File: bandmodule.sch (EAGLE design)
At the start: 16 parts

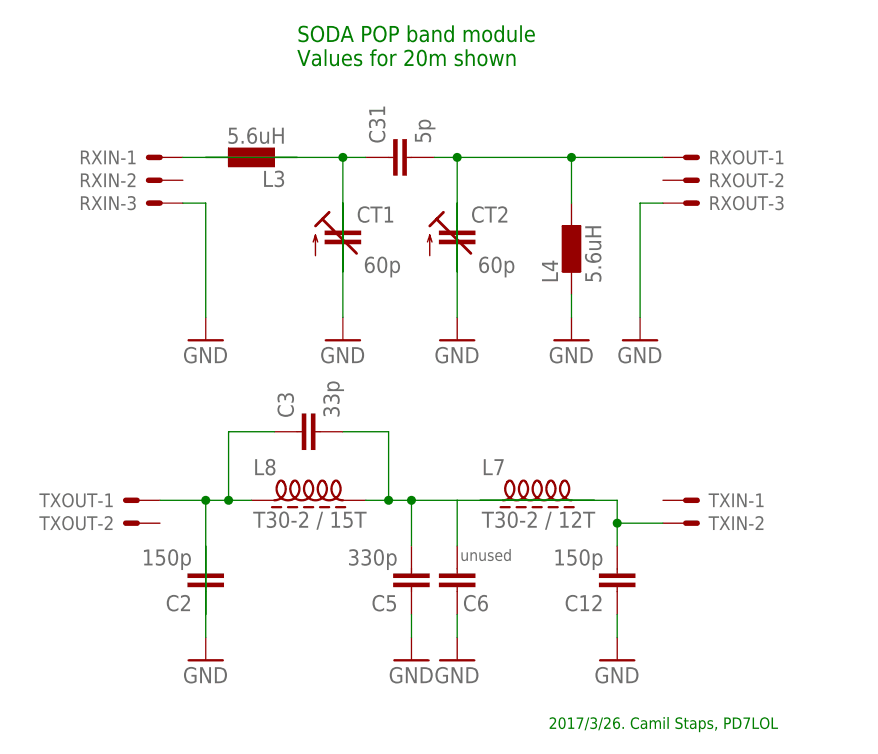
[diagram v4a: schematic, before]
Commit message: Merge C5 and C6 again
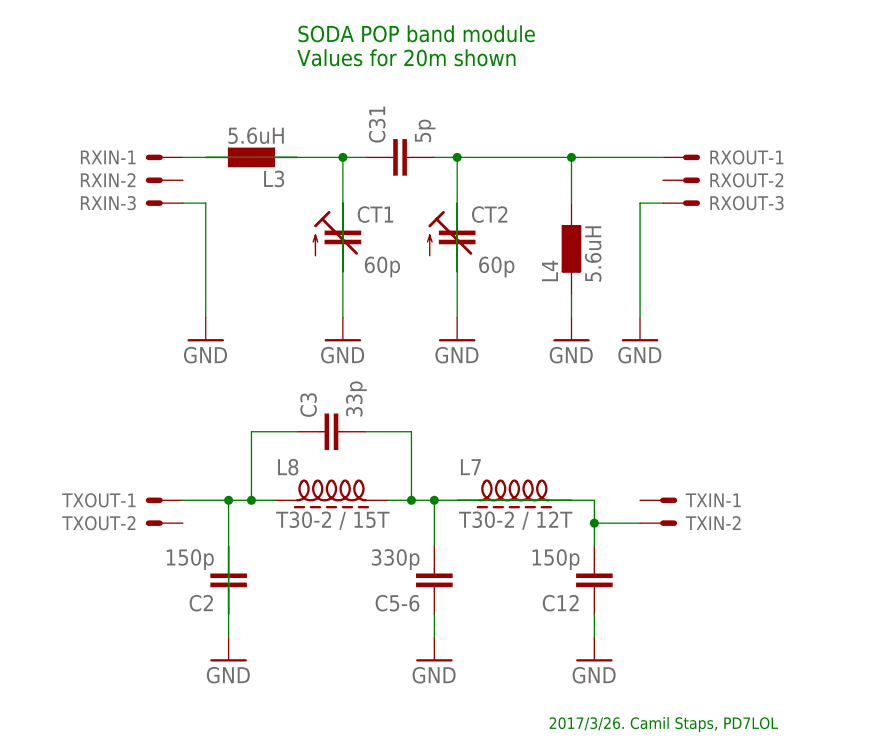
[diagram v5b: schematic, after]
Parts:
- removed C5: 330p, capacitor-wima:C5/2.5
- removed C6: unused, capacitor-wima:C5/2.5
- added C5-6: 330p, capacitor-wima:C5/2.5
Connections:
- net GND: now also C5-6.1; no longer C5.1, C6.1
- net N$5: now also C5-6.2; no longer C5.2, C6.2
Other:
- moved on the sheet: C12, C2, C3, L7, L8, TXIN-1, TXIN-2, TXOUT-1, TXOUT-2
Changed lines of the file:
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@@
 <part name="L8" library="toroids" deviceset="INDUCTOR" device="T30-2-28AWG-12T" value="T30-2 / 15T"/>
 <part name="L7" library="toroids" deviceset="INDUCTOR" device="T30-2-28AWG-12T" value="T30-2 / 12T"/>
-<part name="C5" library="capacitor-wima" deviceset="C" device="5/2.5" value="330p"/>
+<part name="C5-6" library="capacitor-wima" deviceset="C" device="5/2.5" value="330p"/>
 <part name="C12" library="capacitor-wima" deviceset="C" device="5/2.5" value="150p"/>
 <part name="C3" library="capacitor-wima" deviceset="C" device="5/2.5" value="33p"/>
@@
 <part name="L4" library="eagle-ltspice" deviceset="L" device="0207/10" value="5.6uH"/>
 <part name="L3" library="eagle-ltspice" deviceset="L" device="0207/10" value="5.6uH"/>
-<part name="C6" library="capacitor-wima" deviceset="C" device="5/2.5" value="unused"/>
-<part name="GND9" library="supply1" deviceset="GND" device=""/>
 </parts>
 <sheets>
@@
 <instance part="GND4" gate="1" x="48.26" y="45.72"/>
 <instance part="GND5" gate="1" x="60.96" y="45.72"/>
-<instance part="TXIN" gate="-1" x="73.66" y="27.94" smashed="yes">
-<attribute name="NAME" x="76.2" y="27.178" size="1.524" layer="95"/>
+<instance part="TXIN" gate="-1" x="71.12" y="27.94" smashed="yes">
+<attribute name="NAME" x="73.66" y="27.178" size="1.524" layer="95"/>
 </instance>
-<instance part="TXIN" gate="-2" x="73.66" y="25.4"/>
-<instance part="TXOUT" gate="-1" x="12.7" y="27.94" smashed="yes" rot="MR0">
-<attribute name="NAME" x="10.16" y="27.178" size="1.524" layer="95" rot="MR0"/>
+<instance part="TXIN" gate="-2" x="71.12" y="25.4"/>
+<instance part="TXOUT" gate="-1" x="15.24" y="27.94" smashed="yes" rot="MR0">
+<attribute name="NAME" x="12.7" y="27.178" size="1.524" layer="95" rot="MR0"/>
 </instance>
-<instance part="TXOUT" gate="-2" x="12.7" y="25.4" rot="MR0"/>
-<instance part="C2" gate="G$1" x="20.32" y="17.78" rot="R180"/>
-<instance part="L8" gate="G$1" x="30.48" y="27.94"/>
-<instance part="L7" gate="G$1" x="55.88" y="27.94"/>
-<instance part="C5" gate="G$1" x="43.18" y="17.78" smashed="yes" rot="R180">
-<attribute name="NAME" x="41.656" y="17.399" size="1.778" layer="95" rot="R180"/>
-<attribute name="VALUE" x="41.656" y="22.479" size="1.778" layer="96" rot="R180"/>
+<instance part="TXOUT" gate="-2" x="15.24" y="25.4" rot="MR0"/>
+<instance part="C2" gate="G$1" x="22.86" y="17.78" rot="R180"/>
+<instance part="L8" gate="G$1" x="33.02" y="27.94"/>
+<instance part="L7" gate="G$1" x="53.34" y="27.94"/>
+<instance part="C5-6" gate="G$1" x="45.72" y="17.78" smashed="yes" rot="R180">
+<attribute name="NAME" x="44.196" y="17.399" size="1.778" layer="95" rot="R180"/>
+<attribute name="VALUE" x="44.196" y="22.479" size="1.778" layer="96" rot="R180"/>
 </instance>
-<instance part="C12" gate="G$1" x="66.04" y="17.78" rot="R180"/>
-<instance part="C3" gate="G$1" x="30.48" y="35.56" rot="R90"/>
-<instance part="GND6" gate="1" x="20.32" y="10.16"/>
-<instance part="GND7" gate="1" x="43.18" y="10.16"/>
-<instance part="GND8" gate="1" x="66.04" y="10.16"/>
+<instance part="C12" gate="G$1" x="63.5" y="17.78" rot="R180"/>
+<instance part="C3" gate="G$1" x="33.02" y="35.56" rot="R90"/>
+<instance part="GND6" gate="1" x="22.86" y="10.16"/>
+<instance part="GND7" gate="1" x="45.72" y="10.16"/>
+<instance part="GND8" gate="1" x="63.5" y="10.16"/>
 <instance part="L4" gate="G$1" x="60.96" y="55.88"/>
 <instance part="L3" gate="G$1" x="25.4" y="66.04" rot="R90"/>
-<instance part="C6" gate="G$1" x="48.26" y="17.78" smashed="yes" rot="R180">
-<attribute name="NAME" x="51.816" y="17.399" size="1.778" layer="95" rot="R180"/>
-<attribute name="VALUE" x="54.356" y="22.479" size="1.27" layer="96" rot="R180"/>
-</instance>
-<instance part="GND9" gate="1" x="48.26" y="10.16"/>
 </instances>
 <busses>
@@
 <pinref part="C2" gate="G$1" pin="2"/>
 <pinref part="GND6" gate="1" pin="GND"/>
-<wire x1="20.32" y1="22.86" x2="20.32" y2="12.7" width="0.1524" layer="91"/>
+<wire x1="22.86" y1="22.86" x2="22.86" y2="12.7" width="0.1524" layer="91"/>
 </segment>
 <segment>
-<pinref part="C5" gate="G$1" pin="1"/>
+<pinref part="C5-6" gate="G$1" pin="1"/>
 <pinref part="GND7" gate="1" pin="GND"/>
-<wire x1="43.18" y1="15.24" x2="43.18" y2="12.7" width="0.1524" layer="91"/>
+<wire x1="45.72" y1="15.24" x2="45.72" y2="12.7" width="0.1524" layer="91"/>
 </segment>
 <segment>
 <pinref part="C12" gate="G$1" pin="1"/>
 <pinref part="GND8" gate="1" pin="GND"/>
-<wire x1="66.04" y1="15.24" x2="66.04" y2="12.7" width="0.1524" layer="91"/>
-</segment>
-<segment>
-<pinref part="GND9" gate="1" pin="GND"/>
-<pinref part="C6" gate="G$1" pin="1"/>
-<wire x1="48.26" y1="12.7" x2="48.26" y2="15.24" width="0.1524" layer="91"/>
+<wire x1="63.5" y1="15.24" x2="63.5" y2="12.7" width="0.1524" layer="91"/>
 </segment>
 </net>
@@
 <pinref part="L8" gate="G$1" pin="2"/>
 <pinref part="L7" gate="G$1" pin="2"/>
-<wire x1="38.1" y1="27.94" x2="40.64" y2="27.94" width="0.1524" layer="91"/>
-<pinref part="C5" gate="G$1" pin="2"/>
 <wire x1="40.64" y1="27.94" x2="43.18" y2="27.94" width="0.1524" layer="91"/>
-<wire x1="43.18" y1="27.94" x2="48.26" y2="27.94" width="0.1524" layer="91"/>
-<wire x1="48.26" y1="27.94" x2="63.5" y2="27.94" width="0.1524" layer="91"/>
-<wire x1="43.18" y1="27.94" x2="43.18" y2="22.86" width="0.1524" layer="91"/>
+<pinref part="C5-6" gate="G$1" pin="2"/>
+<wire x1="43.18" y1="27.94" x2="45.72" y2="27.94" width="0.1524" layer="91"/>
+<wire x1="45.72" y1="27.94" x2="60.96" y2="27.94" width="0.1524" layer="91"/>
+<wire x1="45.72" y1="27.94" x2="45.72" y2="22.86" width="0.1524" layer="91"/>
 <pinref part="C3" gate="G$1" pin="2"/>
-<wire x1="35.56" y1="35.56" x2="40.64" y2="35.56" width="0.1524" layer="91"/>
-<wire x1="40.64" y1="35.56" x2="40.64" y2="27.94" width="0.1524" layer="91"/>
-<junction x="40.64" y="27.94"/>
+<wire x1="38.1" y1="35.56" x2="43.18" y2="35.56" width="0.1524" layer="91"/>
+<wire x1="43.18" y1="35.56" x2="43.18" y2="27.94" width="0.1524" layer="91"/>
 <junction x="43.18" y="27.94"/>
-<pinref part="C6" gate="G$1" pin="2"/>
-<wire x1="48.26" y1="22.86" x2="48.26" y2="27.94" width="0.1524" layer="91"/>
+<junction x="45.72" y="27.94"/>
 </segment>
 </net>
@@
 <pinref part="L7" gate="G$1" pin="1"/>
 <pinref part="C12" gate="G$1" pin="2"/>
-<wire x1="50.8" y1="27.94" x2="66.04" y2="27.94" width="0.1524" layer="91"/>
-<wire x1="66.04" y1="27.94" x2="66.04" y2="25.4" width="0.1524" layer="91"/>
+<wire x1="48.26" y1="27.94" x2="63.5" y2="27.94" width="0.1524" layer="91"/>
+<wire x1="63.5" y1="27.94" x2="63.5" y2="25.4" width="0.1524" layer="91"/>
 <pinref part="TXIN" gate="-2" pin="S"/>
-<wire x1="66.04" y1="25.4" x2="66.04" y2="22.86" width="0.1524" layer="91"/>
-<wire x1="66.04" y1="25.4" x2="71.12" y2="25.4" width="0.1524" layer="91"/>
-<junction x="66.04" y="25.4"/>
+<wire x1="63.5" y1="25.4" x2="63.5" y2="22.86" width="0.1524" layer="91"/>
+<wire x1="63.5" y1="25.4" x2="68.58" y2="25.4" width="0.1524" layer="91"/>
+<junction x="63.5" y="25.4"/>
 </segment>
 </net>
@@
 <segment>
 <pinref part="C3" gate="G$1" pin="1"/>
-<wire x1="22.86" y1="35.56" x2="27.94" y2="35.56" width="0.1524" layer="91"/>
+<wire x1="25.4" y1="35.56" x2="30.48" y2="35.56" width="0.1524" layer="91"/>
 <pinref part="TXOUT" gate="-1" pin="S"/>
 <pinref part="L8" gate="G$1" pin="1"/>
-<wire x1="15.24" y1="27.94" x2="20.32" y2="27.94" width="0.1524" layer="91"/>
+<wire x1="17.78" y1="27.94" x2="22.86" y2="27.94" width="0.1524" layer="91"/>
 <pinref part="C2" gate="G$1" pin="1"/>
-<wire x1="20.32" y1="27.94" x2="22.86" y2="27.94" width="0.1524" layer="91"/>
 <wire x1="22.86" y1="27.94" x2="25.4" y2="27.94" width="0.1524" layer="91"/>
-<wire x1="20.32" y1="27.94" x2="20.32" y2="15.24" width="0.1524" layer="91"/>
-<wire x1="22.86" y1="35.56" x2="22.86" y2="27.94" width="0.1524" layer="91"/>
-<junction x="20.32" y="27.94"/>
+<wire x1="25.4" y1="27.94" x2="27.94" y2="27.94" width="0.1524" layer="91"/>
+<wire x1="22.86" y1="27.94" x2="22.86" y2="15.24" width="0.1524" layer="91"/>
+<wire x1="25.4" y1="35.56" x2="25.4" y2="27.94" width="0.1524" layer="91"/>
 <junction x="22.86" y="27.94"/>
+<junction x="25.4" y="27.94"/>
 </segment>
 </net>

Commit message: Move L7 and L8 for more space; change artwork
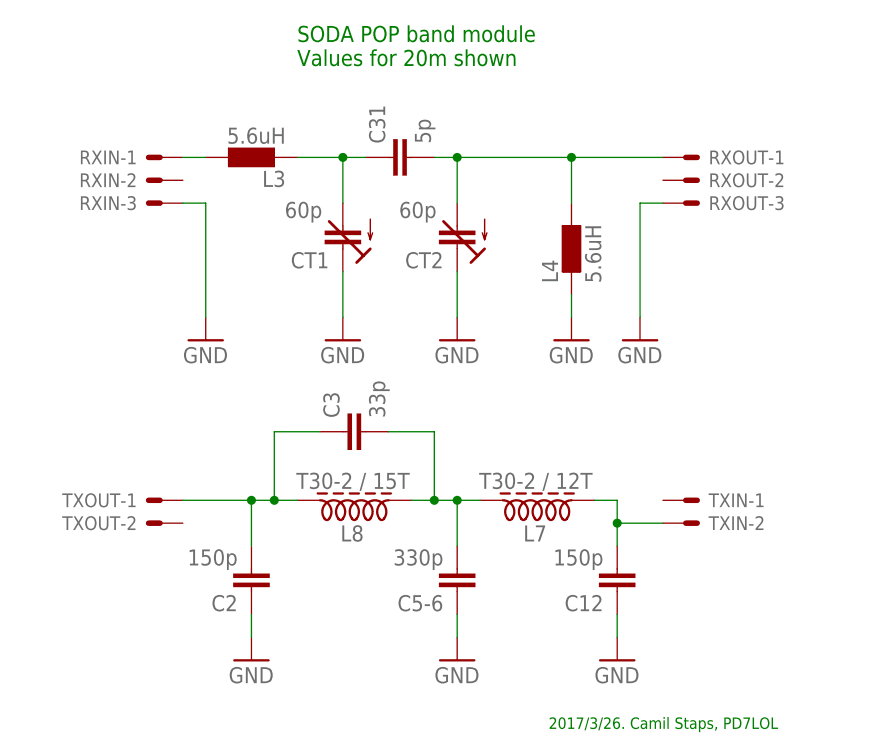
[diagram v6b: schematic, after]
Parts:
- L7, L8: device toroids:INDUCTORT30-2-28AWG-12T -> toroids:INDUCTORT30-2-28AWG-15T
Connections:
- net GND: now also C2.1; no longer C2.2
- net N$1: now also L3.1; no longer L3.2
- net N$2: now also L3.2; no longer L3.1
- net N$5: now also L8.1; no longer L8.2
- net N$8: now also C2.2, L8.2; no longer C2.1, L8.1
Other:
- moved on the sheet: C12, C2, C3, C5-6, CT1, CT2, L7, L8, TXIN-1, TXIN-2
